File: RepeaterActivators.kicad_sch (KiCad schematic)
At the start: 26 parts, among them J1 Conn_01x04_Female RPi, J2 Conn_01x04_Female Radio1, Q1 2N7000, Q2 2N7000, Q3 2N7000, Q4 2N7000, U1 74LS273, U2 74LS04, U3 74LS138, U4 74LS138, U5 74AHC04, U6 74LS04

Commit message: DBD: gitignore + error check fixes
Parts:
- added J3: Conn_01x04_Female Radio2, symbol Connector:Conn_01x04_Female
- added J4, J5: Conn_01x04_Female Mister E, symbol Connector:Conn_01x04_Female
- added Q5, Q6, Q7, Q8: 2N7000, Package_TO_SOT_THT:TO-92_Inline, symbol Transistor_FET:2N7000
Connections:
- net GND: now also U1.20 (VCC), U2.14 (VCC), U3.16 (VCC), U4.16 (VCC), U5.14 (VCC), V1.1 (E1), Q5.1 (S), Q6.1 (S), Q7.1 (S)
- net Radio1 Fan (Add SR Latch? as switch): now also J2.4 (Pin_4), Q4.3 (D)
- net at D7.1 (K): now also Q7.2 (G)
- net at Q4.1 (S), V2.1 (E1): now also Q8.1 (S)
- net at D6.1 (K): now also Q6.2 (G)
- net at D10.1 (K): now also J4.2 (Pin_2)
- net at D9.1 (K): now also J4.1 (Pin_1)
- net at U4.10 (O5): now also J5.2 (Pin_2)
- net at U4.11 (O4): now also J5.1 (Pin_1)
- net at U4.7 (O7): now also J5.4 (Pin_4)
- net at U4.9 (O6): now also J5.3 (Pin_3)
- net at D11.1 (K): now also J4.3 (Pin_3)
- net at D12.1 (K): now also J4.4 (Pin_4)
- net at D5.1 (K): now also Q5.2 (G)
- net at D8.1 (K): now also Q8.2 (G)
- new net: J3.4 (Pin_4), Q8.3 (D)
- new net: J3.1 (Pin_1), Q5.3 (D)
- new net: J3.2 (Pin_2), Q6.3 (D)
- new net: J3.3 (Pin_3), Q7.3 (D)
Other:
- note added: "100mm PCB board width (add 1.5mm tolerance) 1mm thickness on board 40mm between slot shelves 2mm slot shelf overlap with board"

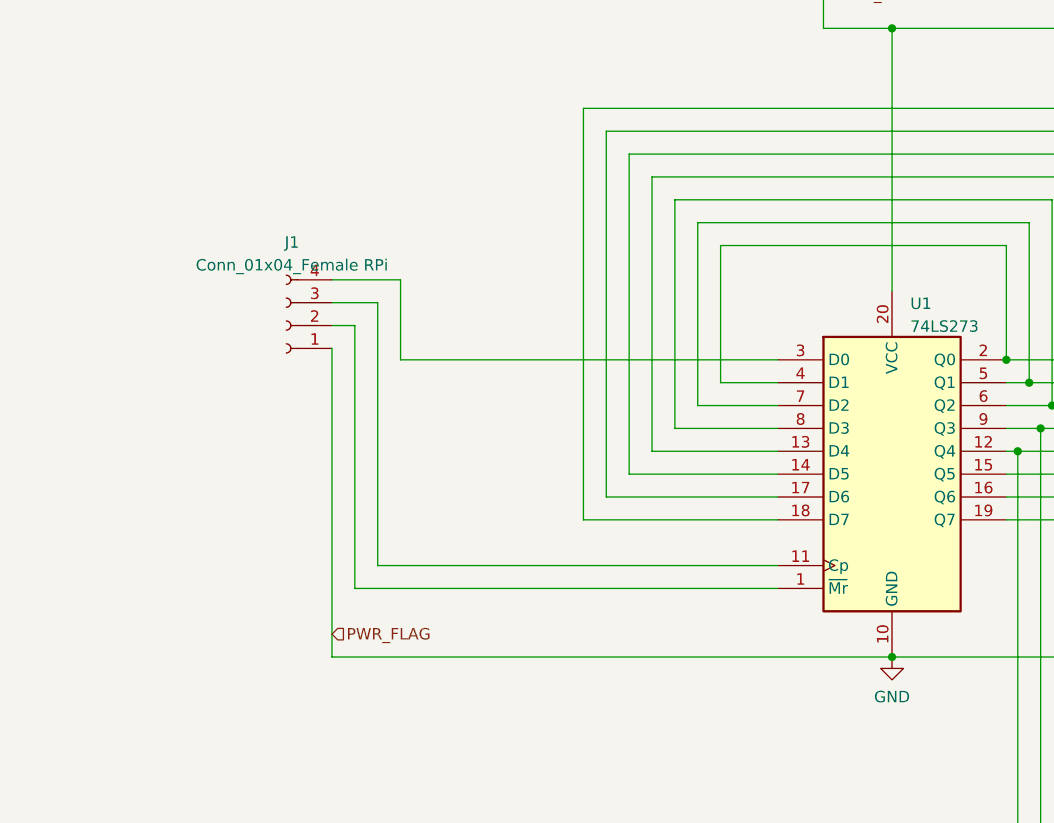
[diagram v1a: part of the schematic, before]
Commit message: DBD: attempt at esd protection, probably look harder at this later
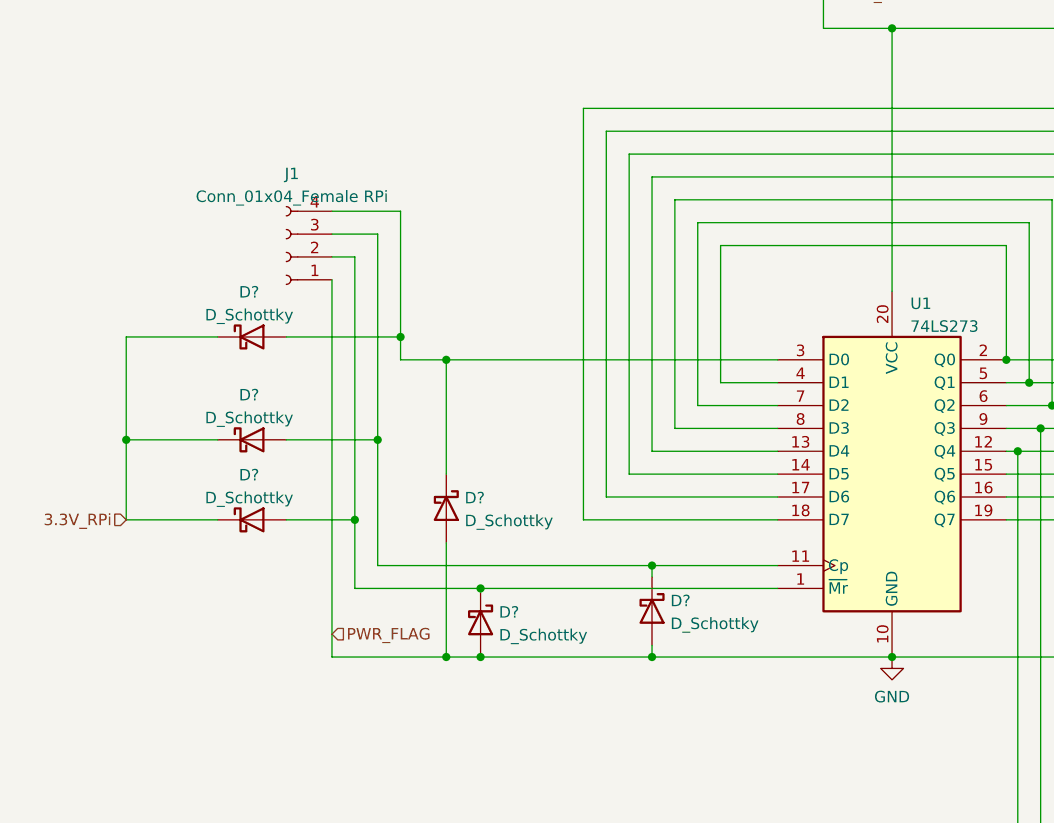
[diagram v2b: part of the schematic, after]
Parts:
- added D? (x6): D_Schottky, symbol Device:D_Schottky
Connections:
- net GND: now also D?.2 (A), D?.2 (A), D?.2 (A)
- net at J1.2 (Pin_2), U1.1 (~{Mr}): now also D?.1 (K), D?.2 (A)
- net at J1.3 (Pin_3), U1.11 (Cp): now also D?.1 (K), D?.2 (A)
- net at J1.4 (Pin_4), U1.3 (D0): now also D?.1 (K), D?.2 (A)
- new net 3.3V_RPi: D?.1 (K), D?.1 (K), D?.1 (K)
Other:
- moved on the sheet: J1

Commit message: DBD: added SN74LS107 JK Flip Flops for persistent activation of fans and ptt's until pi sends a code to de-activate
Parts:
- removed D10, D11, D12, D9: 1N4001, Diode_THT:D_DO-41_SOD81_P10.16mm_Horizontal, symbol Diode:1N4001
- removed J4, J5: Conn_01x04_Female Mister E, symbol Connector:Conn_01x04_Female
- removed V1: 5V, symbol pspice:VSOURCE
- removed V2: 12V, symbol pspice:VSOURCE
- added C?: 0.1u, symbol Device:C
- added C?: 0.33u, symbol Device:C
- added D?: GREEN, symbol Device:LED
- added R? (x9): 1k, symbol Device:R_US
- added R?: 270, symbol Device:R_US
- added U? (x6): 74LS107, symbol 74xx:74LS107
- added U?: L7805, symbol Regulator_Linear:L7805
- gave numbers to parts that had none: 6
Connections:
- net GND: now also D15.2 (A), Q8.1 (S), C?.2, C?.2, R?.2, U?.2 (GND), U?.7 (GND), U?.7 (GND); no longer D18.2 (A), Q5.1 (S), U1.20 (VCC), U2.14 (VCC), U3.16 (VCC), U4.16 (VCC), U5.14 (VCC)
- net Radio1 Frequency Down: now also J2.4 (Pin_4); no longer J2.3 (Pin_3)
- net Radio1 Frequency Up: now also J2.3 (Pin_3); no longer J2.2 (Pin_2)
- net |CLR: now reaches J1.2 (Pin_2), U1.1 (~{Mr})
- net |CLR: now also D14.2 (A), D15.1 (K); no longer D15.2 (A), D17.1 (K)
- net Clock Pulse: now reaches J1.3 (Pin_3), U1.11 (Cp)
- net Clock Pulse: now also D17.1 (K), D18.2 (A); no longer D14.2 (A), D18.1 (K)
- net at D7.1 (K): now also R?.1; no longer Q7.2 (G)
- net at D7.2 (A): now also U?.2 (~{Q}); no longer U5.2
- net +12V: now reaches Q4.1 (S)
- net +12V: now also Q5.1 (S), C?.1, U?.1 (IN); no longer Q8.1 (S)
- net at Q4.2 (G): now also R?.2; no longer D4.1 (K)
- net at Q2.2 (G): now also R?.2; no longer D2.1 (K)
- net at D6.1 (K): now also R?.1; no longer Q6.2 (G)
- net at D6.2 (A): now also U5.4; no longer U2.12
- net at D3.1 (K): now also R?.1; no longer Q3.2 (G)
- net at D3.2 (A): now also U2.8; no longer U2.6
- net at D4.2 (A): now also U2.6; no longer U2.8
- net at D8.1 (K): now also R?.1; no longer Q8.2 (G)
- net at Q8.3 (D): now also J3.3 (Pin_3); no longer J3.4 (Pin_4)
- net Data Input: now reaches D13.2 (A), D16.1 (K), J1.4 (Pin_4), U1.3 (D0)
- net at U2.10: now also U?.12 (C); no longer D5.2 (A)
- net at D1.1 (K): now also R?.1; no longer Q1.2 (G)
- net at U6.2: now also U?.12 (C); no longer D1.2 (A)
- net at D2.2 (A): now also U?.6 (~{Q}); no longer U2.4
- net at J3.1 (Pin_1): now also Q7.3 (D); no longer Q5.3 (D)
- net at J3.2 (Pin_2): now also Q5.3 (D); no longer Q6.3 (D)
- net at Q5.2 (G): now also R?.2; no longer D5.1 (K)
- net at D8.2 (A): now also U?.6 (~{Q}); no longer U5.4
- net 3.3V_RPi renamed +5V
- net +5V: now also D18.1 (K), U1.20 (VCC), U2.14 (VCC), U3.16 (VCC), U4.16 (VCC), U5.14 (VCC), C?.1, R?.1, U?.1 (J), U?.1 (J), U?.10 (~{R}), U?.10 (~{R}), U?.11 (K), U?.11 (K), U?.13 (~{R}), U?.13 (~{R}), U?.14 (VCC), U?.14 (VCC), U?.3 (OUT), U?.4 (K), U?.4 (K), U?.8 (J), U?.8 (J); no longer D15.1 (K)
- net Radio1 Fan (Add SR Latch? as switch) renamed Radio1 Fan
- net Radio1 Fan: now also J2.2 (Pin_2); no longer J2.4 (Pin_4)
- new net: D1.2 (A), U?.2 (~{Q})
- new net: Q3.2 (G), R?.2
- new net: Q8.2 (G), R?.2
- new net: Q6.2 (G), R?.2
- new net: D5.2 (A), U5.2
- new net: U2.12, U?.9 (C)
- new net: D?.1 (K), R?.1
- new net: D?.2 (A), R?.2
- new net: D2.1 (K), R?.1
- new net: Q7.2 (G), R?.2
- new net: J3.4 (Pin_4), Q6.3 (D)
- new net: Q1.2 (G), R?.2
- new net: U2.4, U?.9 (C)
- new net: D4.1 (K), R?.1
- new net: D5.1 (K), R?.1
- no-connect marks 0 -> 12
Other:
- note added: "SN74LS04"
- note added: "SN74LS107"
- note added: "Voltage Regulator (Power Supply)"
- moved on the sheet: D1, D13, D14, D15, D16, D17, D18, D2, D3, D4, D5, D6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

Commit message: DBD: changed rpi connector to 1x6, changing radio connectors to shielded rj-45 with led's
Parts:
- removed J1: Conn_01x04_Female RPi, symbol Connector:Conn_01x04_Female
- added J?: 8PRJ45_LED_Shielded_Radio1, symbol Connector:8P8C_LED_Shielded
- added J?: 8PRJ45_LED_Shielded_Radio2, symbol Connector:8P8C_LED_Shielded
- added J?: Conn_01x06_Female, symbol Connector:Conn_01x06_Female
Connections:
- net Clock Pulse: now also J?.3 (Pin_3)
- net Data Input: now also J?.4 (Pin_4)
- net GND: now also J?.1 (Pin_1), J?.SH, J?.SH
- net |CLR: now also J?.2 (Pin_2)
- new net SPI_RPi_Radio1: J?.6 (Pin_6)
- new net SPI_RPi_Radio2: J?.5 (Pin_5)
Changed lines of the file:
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@@
+    (stroke (width 0) (type default) (color 0 0 0 0))
+  )
+  (wire (pts (xy 41.91 73.66) (xy 52.07 73.66))
     (stroke (width 0) (type default) (color 0 0 0 0))
   )
@@
     (stroke (width 0) (type default) (color 0 0 0 0))
   )
+  (wire (pts (xy 41.91 71.12) (xy 49.53 71.12))
+    (stroke (width 0) (type default) (color 0 0 0 0))
+  )
   (wire (pts (xy 336.55 207.01) (xy 336.55 138.43))
     (stroke (width 0) (type default) (color 0 0 0 0))
@@
     (stroke (width 0) (type default) (color 0 0 0 0))
   )
+  (wire (pts (xy 52.07 60.96) (xy 52.07 73.66))
+    (stroke (width 0) (type default) (color 0 0 0 0))
+  )
   (wire (pts (xy 275.59 78.74) (xy 266.7 78.74))
     (stroke (width 0) (type default) (color 0 0 0 0))
@@
   )
   (wire (pts (xy 220.98 93.98) (xy 236.22 93.98))
+    (stroke (width 0) (type default) (color 0 0 0 0))
+  )
+  (wire (pts (xy 49.53 55.88) (xy 49.53 71.12))
     (stroke (width 0) (type default) (color 0 0 0 0))
   )
@@
   (label "Clock Pulse" (at 43.18 78.74 0)
     (effects (font (size 1.27 1.27)) (justify left bottom))
+  )
+  (global_label "SPI_RPi_Radio2" (shape input) (at 52.07 60.96 0) (fields_autoplaced)
+    (effects (font (size 1.27 1.27)) (justify left))
+    (property "Intersheet References" "${INTERSHEET_REFS}" (id 0) (at 69.1788 60.8806 0)
+      (effects (font (size 1.27 1.27)) (justify left) hide)
+    )
+  )
+  (global_label "SPI_RPi_Radio1" (shape input) (at 49.53 55.88 0) (fields_autoplaced)
+    (effects (font (size 1.27 1.27)) (justify left))
+    (property "Intersheet References" "${INTERSHEET_REFS}" (id 0) (at 66.6388 55.8006 0)
+      (effects (font (size 1.27 1.27)) (justify left) hide)
+    )
   )
   (hierarchical_label "PWR_FLAG" (shape input) (at 161.29 180.34 0)
@@
     (pin "7")
   )
+  (symbol (lib_id "Connector:8P8C_LED_Shielded") (at 388.62 72.39 180) (unit 1)
+    (in_bom yes) (on_board yes) (fields_autoplaced)
+    (property "Reference" "J?" (id 0) (at 388.62 87.1204 0))
+    (property "Value" "8PRJ45_LED_Shielded_Radio1" (id 1) (at 388.62 89.6573 0))
+    (property "Footprint" "" (id 2) (at 388.62 73.025 90)
+      (effects (font (size 1.27 1.27)) hide)
+    )
+    (property "Datasheet" "~" (id 3) (at 388.62 73.025 90)
+      (effects (font (size 1.27 1.27)) hide)
+    )
+    (pin "1")
+    (pin "10")
+    (pin "11")
+    (pin "12")
+    (pin "2")
+    (pin "3")
+    (pin "4")
+    (pin "5")
+    (pin "6")
+    (pin "7")
+    (pin "8")
+    (pin "9")
+    (pin "SH")
+  )
+  (symbol (lib_id "Connector:8P8C_LED_Shielded") (at 388.62 158.75 180) (unit 1)
+    (in_bom yes) (on_board yes) (fields_autoplaced)
+    (property "Reference" "J?" (id 0) (at 388.62 173.4804 0))
+    (property "Value" "8PRJ45_LED_Shielded_Radio2" (id 1) (at 388.62 176.0173 0))
+    (property "Footprint" "" (id 2) (at 388.62 159.385 90)
+      (effects (font (size 1.27 1.27)) hide)
+    )
+    (property "Datasheet" "~" (id 3) (at 388.62 159.385 90)
+      (effects (font (size 1.27 1.27)) hide)
+    )
+    (pin "1")
+    (pin "10")
+    (pin "11")
+    (pin "12")
+    (pin "2")
+    (pin "3")
+    (pin "4")
+    (pin "5")
+    (pin "6")
+    (pin "7")
+    (pin "8")
+    (pin "9")
+    (pin "SH")
+  )
   (symbol (lib_id "Diode:1N4001") (at 300.99 166.37 180) (unit 1)
     (in_bom yes) (on_board yes) (fields_autoplaced)
@@
     (pin "1")
   )
+  (symbol (lib_id "Connector:Conn_01x06_Female") (at 36.83 78.74 180) (unit 1)
+    (in_bom yes) (on_board yes) (fields_autoplaced)
+    (property "Reference" "J?" (id 0) (at 37.465 66.963 0))
+    (property "Value" "Conn_01x06_Female" (id 1) (at 37.465 69.4999 0))
+    (property "Footprint" "" (id 2) (at 36.83 78.74 0)
+      (effects (font (size 1.27 1.27)) hide)
+    )
+    (property "Datasheet" "~" (id 3) (at 36.83 78.74 0)
+      (effects (font (size 1.27 1.27)) hide)
+    )
+    (pin "1")
+    (pin "2")
+    (pin "3")
+    (pin "4")
+    (pin "5")
+    (pin "6")
+  )
   (symbol (lib_id "74xx:74AHC04") (at 213.36 186.69 0) (unit 5)
     (in_bom yes) (on_board yes) (fields_autoplaced)
@@
     (pin "1")
   )
-  (symbol (lib_id "Connector:Conn_01x04_Female") (at 36.83 81.28 180) (unit 1)
-    (in_bom yes) (on_board yes)
-    (property "Reference" "J1" (id 0) (at 36.83 71.12 0))
-    (property "Value" "Conn_01x04_Female RPi" (id 1) (at 36.83 73.66 0))
-    (property "Footprint" "" (id 2) (at 36.83 81.28 0)
-      (effects (font (size 1.27 1.27)) hide)
-    )
-    (property "Datasheet" "~" (id 3) (at 36.83 81.28 0)
-      (effects (font (size 1.27 1.27)) hide)
-    )
-    (pin "1")
-    (pin "2")
-    (pin "3")
-    (pin "4")
-  )
   (symbol (lib_id "74xx:74LS04") (at 213.36 83.82 0) (unit 5)
     (in_bom yes) (on_board yes) (fields_autoplaced)
@@
     (pin "1")
   )
+  (symbol (lib_id "power:GND") (at 388.62 146.05 180) (unit 1)
+    (in_bom yes) (on_board yes) (fields_autoplaced)
+    (property "Reference" "#PWR?" (id 0) (at 388.62 139.7 0)
+      (effects (font (size 1.27 1.27)) hide)
+    )
+    (property "Value" "GND" (id 1) (at 388.62 142.4742 0))
+    (property "Footprint" "" (id 2) (at 388.62 146.05 0)
+      (effects (font (size 1.27 1.27)) hide)
+    )
+    (property "Datasheet" "" (id 3) (at 388.62 146.05 0)
+      (effects (font (size 1.27 1.27)) hide)
+    )
+    (pin "1")
+  )
   (symbol (lib_id "power:GND") (at 285.75 232.41 0) (unit 1)
     (in_bom yes) (on_board yes) (fields_autoplaced)
@@
     (pin "1")
     (pin "2")
+  )
+  (symbol (lib_id "power:GND") (at 388.62 59.69 180) (unit 1)
+    (in_bom yes) (on_board yes) (fields_autoplaced)
+    (property "Reference" "#PWR?" (id 0) (at 388.62 53.34 0)
+      (effects (font (size 1.27 1.27)) hide)
+    )
+    (property "Value" "GND" (id 1) (at 388.62 56.1142 0))
+    (property "Footprint" "" (id 2) (at 388.62 59.69 0)
+      (effects (font (size 1.27 1.27)) hide)
+    )
+    (property "Datasheet" "" (id 3) (at 388.62 59.69 0)
+      (effects (font (size 1.27 1.27)) hide)
+    )
+    (pin "1")
   )
   (symbol (lib_id "74xx:74LS138") (at 161.29 162.56 0) (unit 1)
@@
       (reference "#PWR?") (unit 1) (value "GND") (footprint "")
     )
+    (path "/bfd2f47b-dbd7-4db9-9c56-c5c1ed32e49a"
+      (reference "#PWR?") (unit 1) (value "GND") (footprint "")
+    )
     (path "/bffdf0ce-c255-4f7b-adb1-ca32abccaa82"
       (reference "#PWR?") (unit 1) (value "GND") (footprint "")
     )
+    (path "/c8196bc0-1a5e-404a-96ea-ef1475a77aa5"
+      (reference "#PWR?") (unit 1) (value "GND") (footprint "")
+    )
     (path "/d1d6ca16-cd27-46bf-aae5-467b59ca6e5f"
       (reference "#PWR?") (unit 1) (value "GND") (footprint "")
@@
       (reference "D?") (unit 1) (value "GREEN") (footprint "")
     )
-    (path "/59e5a3c7-b76a-43da-9e9b-4f193ac8ef9c"
-      (reference "J1") (unit 1) (value "Conn_01x04_Female RPi") (footprint "")
-    )
     (path "/b73a8d9e-f9a1-4e59-820c-3e5e2e0bf328"
       (reference "J2") (unit 1) (value "Conn_01x04_Female Radio1") (footprint "")
@@
       (reference "J3") (unit 1) (value "Conn_01x04_Female Radio2") (footprint "")
     )
+    (path "/0e8893fe-7c69-4208-b877-cdaf89618e50"
+      (reference "J?") (unit 1) (value "8PRJ45_LED_Shielded_Radio1") (footprint "")
+    )
+    (path "/11868179-aa7f-42f2-9185-87b72b5fc7a0"
+      (reference "J?") (unit 1) (value "8PRJ45_LED_Shielded_Radio2") (footprint "")
+    )
+    (path "/4cf104ab-d36a-4b23-a23a-f94e19f666e1"
+      (reference "J?") (unit 1) (value "Conn_01x06_Female") (footprint "")
+    )
     (path "/cd3d77a4-fb3e-4cb0-99fa-c24b85c4f625"

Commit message: DBD: converted connectors to rj-45 ethernet, added audio jack input for mic audio with low pass filter, added 2 2 pin connectors for radio fans
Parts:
- removed J2: Conn_01x04_Female Radio1, symbol Connector:Conn_01x04_Female
- removed J3: Conn_01x04_Female Radio2, symbol Connector:Conn_01x04_Female
- added C? (x2): 1n, symbol Device:C
- added FB?: FerriteBead, symbol Device:FerriteBead
- added J?: Conn_01x02_Female, symbol Connector:Conn_01x02_Female
- added J?: AudioJack1_Grounded, symbol Connector:AudioJack2_Ground
- added J?: AudioJack2_Grounded, symbol Connector:AudioJack2_Ground
- added R? (x4): 1k, symbol Device:R_US
- added R? (x2): 3k, symbol Device:R_US
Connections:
- net +12V: now also FB?.1; no longer U?.1 (IN)
- net GND: now also J?.5, J?.5, J?.8, J?.8, C?.2, C?.2, J?.2 (Pin_2), J?.G, J?.G, R?.1, R?.1, R?.2, R?.2
- net Radio1 Fan: now also J?.1 (Pin_1)
- net Radio1 Frequency Down: now also J?.3, Q2.3 (D); no longer Q3.3 (D)
- net Radio1 Frequency Up: now also J?.4, Q3.3 (D); no longer Q2.3 (D)
- net Radio1 PTT: now also J?.7
- net SPI_RPi_Radio1: now also J?.1, J?.12
- net SPI_RPi_Radio2: now also J?.1, J?.12
- net Audio_RPi_Radio1: now reaches J?.10
- net Audio_RPi_Radio1: now also J?.6, C?.1, R?.2
- net at J?.11: now also R?.1 (x2)
- net at J?.9: now also R?.2 (x2)
- net Audio_RPi_Radio2: now reaches J?.10
- net Audio_RPi_Radio2: now also J?.6, C?.1, R?.2
- net at J?.3: now also Q8.3 (D)
- net at J?.4: now also Q6.3 (D)
- net at J?.7: now also Q7.3 (D)
- new net: J?.T, R?.1 (x2)
- new net: FB?.2, U?.1 (IN)
- no-connect marks 12 -> 16
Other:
- note added: "A typical NBFM radio has an unfiltered response from zero to some 8 kHz Reference: https://www.amsat.org/amsat/articles/g3ruh/109.html"
- note added: "Input Audio Jack Connections"
- note added: "This should allow for ~53KHz signals to pass through."
- moved on the sheet: J?
